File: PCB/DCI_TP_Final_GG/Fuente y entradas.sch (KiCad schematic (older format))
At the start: 27 parts, among them J401 IN - Driver A, J402 IN - Driver B, J403 Vin, J404 Vout, U401 LM317

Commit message: Agrego codigos de catalogo
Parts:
- C401, C402: Descripcion UFW1V470MDD -> CAP Electrolitico 47UF 35V RADIAL; digikey# (none) -> 493-11044-1-ND; manf (none) -> Nichicon; manf# (none) -> UFW1V470MDD1TD
- C403: Descripcion (none) -> CAP CER 0.1UF 35V; digikey# (none) -> 587-3364-1-ND; manf (none) -> Taiyo Yuden; manf# (none) -> GMK212BJ104KGHT
- C404, C405: Descripcion C0805C105Z8VACTU -> CAP CER 1UF 10V; digikey# (none) -> 399-1172-1-ND; manf (none) -> KEMET; manf# (none) -> C0805C105K8RACTU
- D401: Descripcion (none) -> LED GREEN 3MM ROUND; digikey# (none) -> 1516-1350-ND; manf (none) -> QT Brightek (QTB); manf# (none) -> QBL7IG60D
- J401, J402: Descripcion (none) -> Tira de Pines 1x10 2.54mm; digikey# (none) -> WM20125-ND; manf (none) -> Molex; manf# (none) -> 0423751863
- J403: Descripcion (none) -> Terminal Block x 2 5MM PCB; digikey# (none) -> 277-1258-ND; manf (none) -> Phoenix Contact; manf# (none) -> 1715022
- J404: Descripcion (none) -> Tira de Pines 1x2 2.54mm; digikey# (none) -> 952-2262-ND; manf (none) -> Harwin Inc.; manf# (none) -> M20-9990246
- JP401: Descripcion (none) -> RES SMD 0 OHM JUMPER; digikey# (none) -> CR0805-J/-000ELFCT-ND; manf (none) -> Bourns Inc.; manf# (none) -> CR0805-J/-000ELF
- R401, R402, R403, R404: Descripcion (none) -> RES 10K OHM SMD 0805; digikey# (none) -> 311-10KARCT-ND; manf (none) -> Yageo; manf# (none) -> RC0805JR-0710KL
- R405, R406, R407, R408, R412: Descripcion (none) -> RES 1k OHM SMD 0805; digikey# (none) -> 311-1.00CRCT-ND; manf (none) -> Yageo; manf# (none) -> RC0805FR-071RL
- R409: Descripcion (none) -> RES 390 OHM SMD 0805; digikey# (none) -> 311-390CRCT-ND; manf (none) -> Yageo; manf# (none) -> RC0805FR-07390RL
- R410: Descripcion (none) -> RES 330 OHM SMD 0805; digikey# (none) -> 311-330CRCT-ND; manf (none) -> Yageo; manf# (none) -> RC0805FR-07330RL
- R411: Descripcion (none) -> RES 240 OHM SMD 0805; digikey# (none) -> 311-.24SCT-ND; manf (none) -> Yageo; manf# (none) -> RL0805FR-070R24L
- U401: Descripcion (none) -> Regulador de tension lineal LM317 SMD SOT-223; digikey# (none) -> LM317MSTT3GOSCT-ND; manf (none) -> ON Semiconductor; manf# (none) -> LM317MSTT3G
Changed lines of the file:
@@
 Title "Replica Dual EasyDriver v4.5"
 Date "2019-10-02"
-Rev ""
+Rev "Matias Brignone"
 Comp "Gonzalo Gontad - CESE-FIUBA"
 Comment1 ""
@@
 F 2 "Package_TO_SOT_SMD:SOT-223-3_TabPin2" H 7400 2350 50  0001 C CIN
 F 3 "http://www.ti.com/lit/ds/symlink/lm317.pdf" H 7400 2100 50  0001 C CNN
+F 4 "Regulador de tension lineal LM317 SMD SOT-223" H 7400 2100 50  0001 C CNN "Descripcion"
+F 5 "LM317MSTT3GOSCT-ND" H 7400 2100 50  0001 C CNN "digikey#"
+F 6 "ON Semiconductor" H 7400 2100 50  0001 C CNN "manf"
+F 7 "LM317MSTT3G" H 7400 2100 50  0001 C CNN "manf#"
 	1    7400 2100
 	1    0    0    -1
@@
 F 2 "TerminalBlock_Phoenix:TerminalBlock_Phoenix_MKDS-1,5-2_1x02_P5.00mm_Horizontal" H 4450 2200 50  0001 C CNN
 F 3 "~" H 4450 2200 50  0001 C CNN
+F 4 "Terminal Block x 2  5MM PCB" H 4450 2200 50  0001 C CNN "Descripcion"
+F 5 "277-1258-ND" H 4450 2200 50  0001 C CNN "digikey#"
+F 6 "Phoenix Contact" H 4450 2200 50  0001 C CNN "manf"
+F 7 "1715022" H 4450 2200 50  0001 C CNN "manf#"
 	1    4450 2200
 	-1   0    0    1
@@
 F 2 "Connector_PinHeader_2.54mm:PinHeader_1x02_P2.54mm_Vertical" H 10100 2100 50  0001 C CNN
 F 3 "~" H 10100 2100 50  0001 C CNN
+F 4 "Tira de Pines 1x2 2.54mm" H 10100 2100 50  0001 C CNN "Descripcion"
+F 5 "952-2262-ND" H 10100 2100 50  0001 C CNN "digikey#"
+F 6 "Harwin Inc." H 10100 2100 50  0001 C CNN "manf"
+F 7 "M20-9990246" H 10100 2100 50  0001 C CNN "manf#"
 	1    10100 2100
 	1    0    0    -1
@@
 F 2 "Capacitor_THT:CP_Radial_D5.0mm_P2.00mm" H 5138 2150 50  0001 C CNN
 F 3 "https://ar.mouser.com/datasheet/2/293/e-ufw-1511690.pdf" H 5100 2300 50  0001 C CNN
-F 4 "UFW1V470MDD" H 5100 2300 50  0001 C CNN "Descripcion"
+F 4 "CAP Electrolitico 47UF  35V RADIAL" H 5100 2300 50  0001 C CNN "Descripcion"
+F 5 "493-11044-1-ND" H 5100 2300 50  0001 C CNN "digikey#"
+F 6 "Nichicon" H 5100 2300 50  0001 C CNN "manf"
+F 7 "UFW1V470MDD1TD" H 5100 2300 50  0001 C CNN "manf#"
 	1    5100 2300
 	1    0    0    -1
@@
 F 2 "Capacitor_SMD:C_0805_2012Metric" H 6488 2150 50  0001 C CNN
 F 3 "https://ar.mouser.com/datasheet/2/212/KEM_C1002_X7R_SMD-1102033.pdf" H 6450 2300 50  0001 C CNN
+F 4 "CAP CER 0.1UF 35V " H 6450 2300 50  0001 C CNN "Descripcion"
+F 5 "587-3364-1-ND" H 6450 2300 50  0001 C CNN "digikey#"
+F 6 "Taiyo Yuden" H 6450 2300 50  0001 C CNN "manf"
+F 7 "GMK212BJ104KGHT" H 6450 2300 50  0001 C CNN "manf#"
 	1    6450 2300
 	1    0    0    -1
@@
 F 2 "Resistor_SMD:R_0805_2012Metric" V 7980 2350 50  0001 C CNN
 F 3 "" H 8050 2350 50  0001 C CNN
+F 4 "RES 240 OHM SMD 0805" H 8050 2350 50  0001 C CNN "Descripcion"
+F 5 "311-.24SCT-ND" H 8050 2350 50  0001 C CNN "digikey#"
+F 6 "Yageo" H 8050 2350 50  0001 C CNN "manf"
+F 7 "RL0805FR-070R24L" H 8050 2350 50  0001 C CNN "manf#"
 	1    8050 2350
 	1    0    0    -1
@@
 F 2 "Resistor_SMD:R_0805_2012Metric" V 7330 2800 50  0001 C CNN
 F 3 "" H 7400 2800 50  0001 C CNN
+F 4 "RES 390 OHM SMD 0805" H 7400 2800 50  0001 C CNN "Descripcion"
+F 5 "311-390CRCT-ND" H 7400 2800 50  0001 C CNN "digikey#"
+F 6 "Yageo" H 7400 2800 50  0001 C CNN "manf"
+F 7 "RC0805FR-07390RL" H 7400 2800 50  0001 C CNN "manf#"
 	1    7400 2800
 	1    0    0    -1
@@
 F 2 "Resistor_SMD:R_0805_2012Metric" V 7330 3250 50  0001 C CNN
 F 3 "" H 7400 3250 50  0001 C CNN
+F 4 "RES 330 OHM SMD 0805" H 7400 3250 50  0001 C CNN "Descripcion"
+F 5 "311-330CRCT-ND" H 7400 3250 50  0001 C CNN "digikey#"
+F 6 "Yageo" H 7400 3250 50  0001 C CNN "manf"
+F 7 "RC0805FR-07330RL" H 7400 3250 50  0001 C CNN "manf#"
 	1    7400 3250
 	1    0    0    -1
@@
 F 2 "Capacitor_SMD:C_0805_2012Metric" H 8538 2150 50  0001 C CNN
 F 3 "https://ar.mouser.com/datasheet/2/212/KEM_C1005_Y5V_SMD-1101305.pdf" H 8500 2300 50  0001 C CNN
-F 4 "C0805C105Z8VACTU" H 8500 2300 50  0001 C CNN "Descripcion"
+F 4 "CAP CER 1UF 10V " H 8500 2300 50  0001 C CNN "Descripcion"
+F 5 "399-1172-1-ND" H 8500 2300 50  0001 C CNN "digikey#"
+F 6 "KEMET" H 8500 2300 50  0001 C CNN "manf"
+F 7 "C0805C105K8RACTU" H 8500 2300 50  0001 C CNN "manf#"
 	1    8500 2300
 	1    0    0    -1
@@
 F 2 "Resistor_SMD:R_0805_2012Metric" V 9480 2300 50  0001 C CNN
 F 3 "" H 9550 2300 50  0001 C CNN
+F 4 "RES 1k OHM SMD 0805" H 9550 2300 50  0001 C CNN "Descripcion"
+F 5 "311-1.00CRCT-ND" H 9550 2300 50  0001 C CNN "digikey#"
+F 6 "Yageo" H 9550 2300 50  0001 C CNN "manf"
+F 7 "RC0805FR-071RL" H 9550 2300 50  0001 C CNN "manf#"
 	1    9550 2300
 	1    0    0    -1
@@
 F 2 "LED_THT:LED_D3.0mm" H 9550 2700 50  0001 C CNN
 F 3 "~" H 9550 2700 50  0001 C CNN
+F 4 "LED GREEN 3MM ROUND " H 9550 2700 50  0001 C CNN "Descripcion"
+F 5 "1516-1350-ND" H 9550 2700 50  0001 C CNN "digikey#"
+F 6 "QT Brightek (QTB)" H 9550 2700 50  0001 C CNN "manf"
+F 7 "QBL7IG60D" H 9550 2700 50  0001 C CNN "manf#"
 	1    9550 2700
 	0    -1   -1   0
@@
 F 2 "Resistor_SMD:R_0805_2012Metric" H 7800 3050 50  0001 C CNN
 F 3 "" H 7800 3050 50  0001 C CNN
+F 4 "RES SMD 0 OHM JUMPER " H 7800 3050 50  0001 C CNN "Descripcion"
+F 5 "CR0805-J/-000ELFCT-ND" H 7800 3050 50  0001 C CNN "digikey#"
+F 6 "Bourns Inc." H 7800 3050 50  0001 C CNN "manf"
+F 7 "CR0805-J/-000ELF" H 7800 3050 50  0001 C CNN "manf#"
 	1    7800 3050
 	1    0    0    -1
@@
 F 2 "Connector_PinHeader_2.54mm:PinHeader_1x10_P2.54mm_Vertical" H 3000 4100 50  0001 C CNN
 F 3 "" H 3000 4100 50  0001 C CNN
+F 4 "Tira de Pines 1x10 2.54mm" H 3000 4100 50  0001 C CNN "Descripcion"
+F 5 "WM20125-ND" H 3000 4100 50  0001 C CNN "digikey#"
+F 6 "Molex" H 3000 4100 50  0001 C CNN "manf"
+F 7 "0423751863" H 3000 4100 50  0001 C CNN "manf#"
 	1    3000 4100
 	-1   0    0    1
@@
 F 2 "Connector_PinHeader_2.54mm:PinHeader_1x10_P2.54mm_Vertical" H 3000 5900 50  0001 C CNN
 F 3 "~" H 3000 5900 50  0001 C CNN
+F 4 "Tira de Pines 1x10 2.54mm" H 3000 5900 50  0001 C CNN "Descripcion"
+F 5 "WM20125-ND" H 3000 5900 50  0001 C CNN "digikey#"
+F 6 "Molex" H 3000 5900 50  0001 C CNN "manf"
+F 7 "0423751863" H 3000 5900 50  0001 C CNN "manf#"
 	1    3000 5900
 	-1   0    0    1
@@
 F 2 "Resistor_SMD:R_0805_2012Metric" V 4230 4300 50  0001 C CNN
 F 3 "" H 4300 4300 50  0001 C CNN
+F 4 "RES 10K OHM SMD 0805" H 4300 4300 50  0001 C CNN "Descripcion"
+F 5 "311-10KARCT-ND" H 4300 4300 50  0001 C CNN "digikey#"
+F 6 "Yageo" H 4300 4300 50  0001 C CNN "manf"
+F 7 "RC0805JR-0710KL" H 4300 4300 50  0001 C CNN "manf#"
 	1    4300 4300
 	1    0    0    -1
@@
 F 2 "Resistor_SMD:R_0805_2012Metric" V 4530 3750 50  0001 C CNN
 F 3 "~" H 4600 3750 50  0001 C CNN
+F 4 "RES 1k OHM SMD 0805" H 4600 3750 50  0001 C CNN "Descripcion"
+F 5 "311-1.00CRCT-ND" H 4600 3750 50  0001 C CNN "digikey#"
+F 6 "Yageo" H 4600 3750 50  0001 C CNN "manf"
+F 7 "RC0805FR-071RL" H 4600 3750 50  0001 C CNN "manf#"
 	1    4600 3750
 	0    1    1    0
@@
 F 2 "Resistor_SMD:R_0805_2012Metric" V 4030 4300 50  0001 C CNN
 F 3 "" H 4100 4300 50  0001 C CNN
+F 4 "RES 10K OHM SMD 0805" H 4100 4300 50  0001 C CNN "Descripcion"
+F 5 "311-10KARCT-ND" H 4100 4300 50  0001 C CNN "digikey#"
+F 6 "Yageo" H 4100 4300 50  0001 C CNN "manf"
+F 7 "RC0805JR-0710KL" H 4100 4300 50  0001 C CNN "manf#"
 	1    4100 4300
 	1    0    0    -1
@@
 F 2 "Resistor_SMD:R_0805_2012Metric" V 4530 4000 50  0001 C CNN
 F 3 "~" H 4600 4000 50  0001 C CNN
+F 4 "RES 1k OHM SMD 0805" H 4600 4000 50  0001 C CNN "Descripcion"
+F 5 "311-1.00CRCT-ND" H 4600 4000 50  0001 C CNN "digikey#"
+F 6 "Yageo" H 4600 4000 50  0001 C CNN "manf"
+F 7 "RC0805FR-071RL" H 4600 4000 50  0001 C CNN "manf#"
 	1    4600 4000
 	0    1    1    0
@@
 F 2 "Resistor_SMD:R_0805_2012Metric" V 4280 6100 50  0001 C CNN
 F 3 "" H 4350 6100 50  0001 C CNN
+F 4 "RES 10K OHM SMD 0805" H 4350 6100 50  0001 C CNN "Descripcion"
+F 5 "311-10KARCT-ND" H 4350 6100 50  0001 C CNN "digikey#"
+F 6 "Yageo" H 4350 6100 50  0001 C CNN "manf"
+F 7 "RC0805JR-0710KL" H 4350 6100 50  0001 C CNN "manf#"
 	1    4350 6100
 	1    0    0    -1
@@
 F 2 "Resistor_SMD:R_0805_2012Metric" V 4580 5550 50  0001 C CNN
 F 3 "~" H 4650 5550 50  0001 C CNN
+F 4 "RES 1k OHM SMD 0805" H 4650 5550 50  0001 C CNN "Descripcion"
+F 5 "311-1.00CRCT-ND" H 4650 5550 50  0001 C CNN "digikey#"
+F 6 "Yageo" H 4650 5550 50  0001 C CNN "manf"
+F 7 "RC0805FR-071RL" H 4650 5550 50  0001 C CNN "manf#"
 	1    4650 5550
 	0    1    1    0
@@
 F 2 "Resistor_SMD:R_0805_2012Metric" V 4080 6100 50  0001 C CNN
 F 3 "" H 4150 6100 50  0001 C CNN
+F 4 "RES 10K OHM SMD 0805" H 4150 6100 50  0001 C CNN "Descripcion"
+F 5 "311-10KARCT-ND" H 4150 6100 50  0001 C CNN "digikey#"
+F 6 "Yageo" H 4150 6100 50  0001 C CNN "manf"
+F 7 "RC0805JR-0710KL" H 4150 6100 50  0001 C CNN "manf#"
 	1    4150 6100
 	1    0    0    -1
@@
 F 2 "Resistor_SMD:R_0805_2012Metric" V 4580 5800 50  0001 C CNN
 F 3 "~" H 4650 5800 50  0001 C CNN
+F 4 "RES 1k OHM SMD 0805" H 4650 5800 50  0001 C CNN "Descripcion"
+F 5 "311-1.00CRCT-ND" H 4650 5800 50  0001 C CNN "digikey#"
+F 6 "Yageo" H 4650 5800 50  0001 C CNN "manf"
+F 7 "RC0805FR-071RL" H 4650 5800 50  0001 C CNN "manf#"
 	1    4650 5800
 	0    1    1    0
@@
 F 2 "Capacitor_THT:CP_Radial_D5.0mm_P2.00mm" H 5788 2150 50  0001 C CNN
 F 3 "https://ar.mouser.com/datasheet/2/293/e-ufw-1511690.pdf" H 5750 2300 50  0001 C CNN
-F 4 "UFW1V470MDD" H 5750 2300 50  0001 C CNN "Descripcion"
+F 4 "CAP Electrolitico 47UF  35V RADIAL" H 5750 2300 50  0001 C CNN "Descripcion"
+F 5 "493-11044-1-ND" H 5750 2300 50  0001 C CNN "digikey#"
+F 6 "Nichicon" H 5750 2300 50  0001 C CNN "manf"
+F 7 "UFW1V470MDD1TD" H 5750 2300 50  0001 C CNN "manf#"
 	1    5750 2300
 	1    0    0    -1
@@
 F 2 "Capacitor_SMD:C_0805_2012Metric" H 9088 2150 50  0001 C CNN
 F 3 "https://ar.mouser.com/datasheet/2/212/KEM_C1005_Y5V_SMD-1101305.pdf" H 9050 2300 50  0001 C CNN
-F 4 "C0805C105Z8VACTU" H 9050 2300 50  0001 C CNN "Descripcion"
+F 4 "CAP CER 1UF 10V " H 9050 2300 50  0001 C CNN "Descripcion"
+F 5 "399-1172-1-ND" H 9050 2300 50  0001 C CNN "digikey#"
+F 6 "KEMET" H 9050 2300 50  0001 C CNN "manf"
+F 7 "C0805C105K8RACTU" H 9050 2300 50  0001 C CNN "manf#"
 	1    9050 2300
 	1    0    0    -1

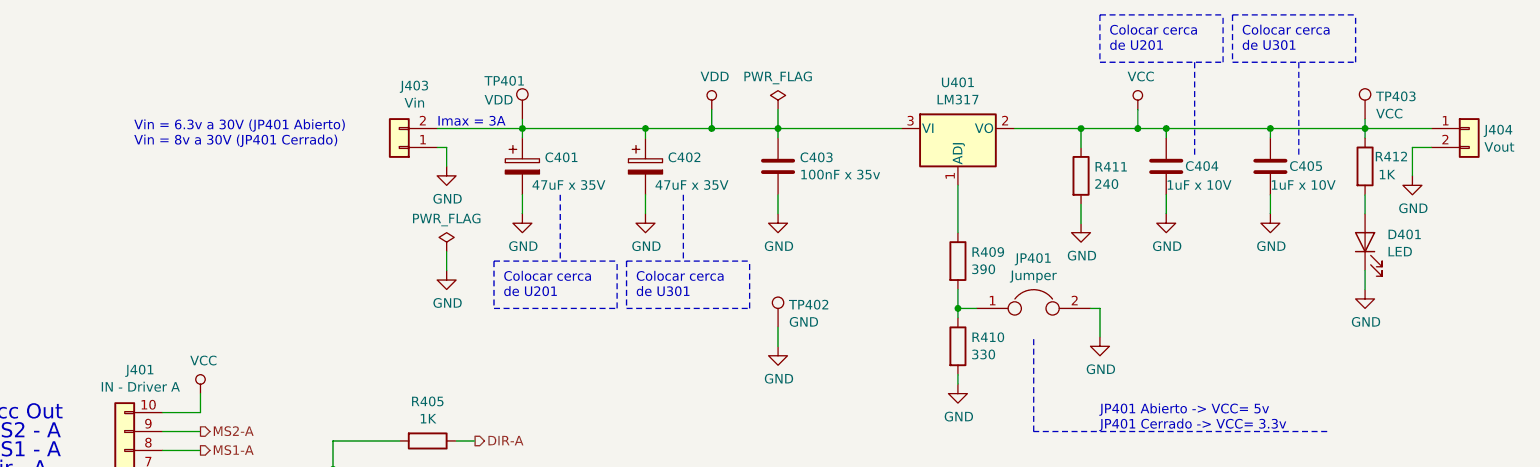
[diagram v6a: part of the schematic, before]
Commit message: Cambio de ubicacion de capacitores de desacople en la jerarquia del esquematico y actualizacion de identificadores en PCB
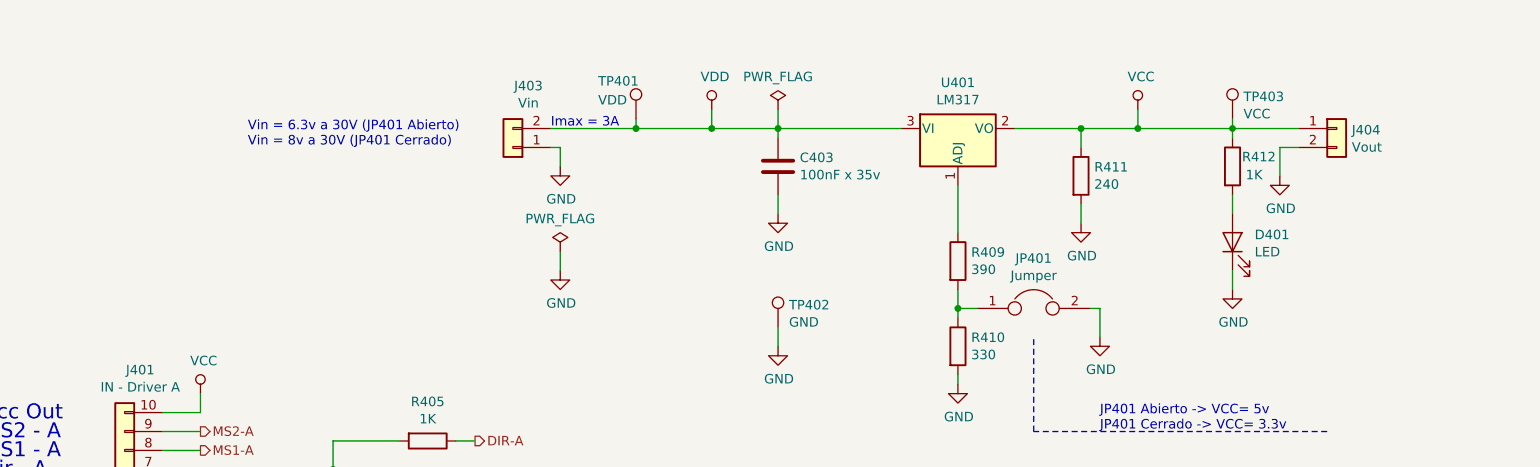
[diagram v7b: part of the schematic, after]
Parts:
- removed C401, C402: 47uF x 35V, Capacitor_THT:CP_Radial_D5.0mm_P2.00mm, symbol Device:CP
- removed C404, C405: 1uF x 10V, Capacitor_SMD:C_0805_2012Metric, symbol Device:C
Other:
- note removed: "Colocar cerca\nde U201"
- note removed: "Colocar cerca\nde U301\n"
- moved on the sheet: D401, J403, J404, R412, TP401, TP403
